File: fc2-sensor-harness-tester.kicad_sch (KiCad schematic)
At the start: 29 parts, among them J1 Conn_01x03_Pin, J105 CTRL INPUT (0-24VDC), J2 Conn_01x03_Pin, J201 0-10V DIM +, J203 V_IN (-) / 0-10V (-), Q203 BC858, Q205 DZT2222A

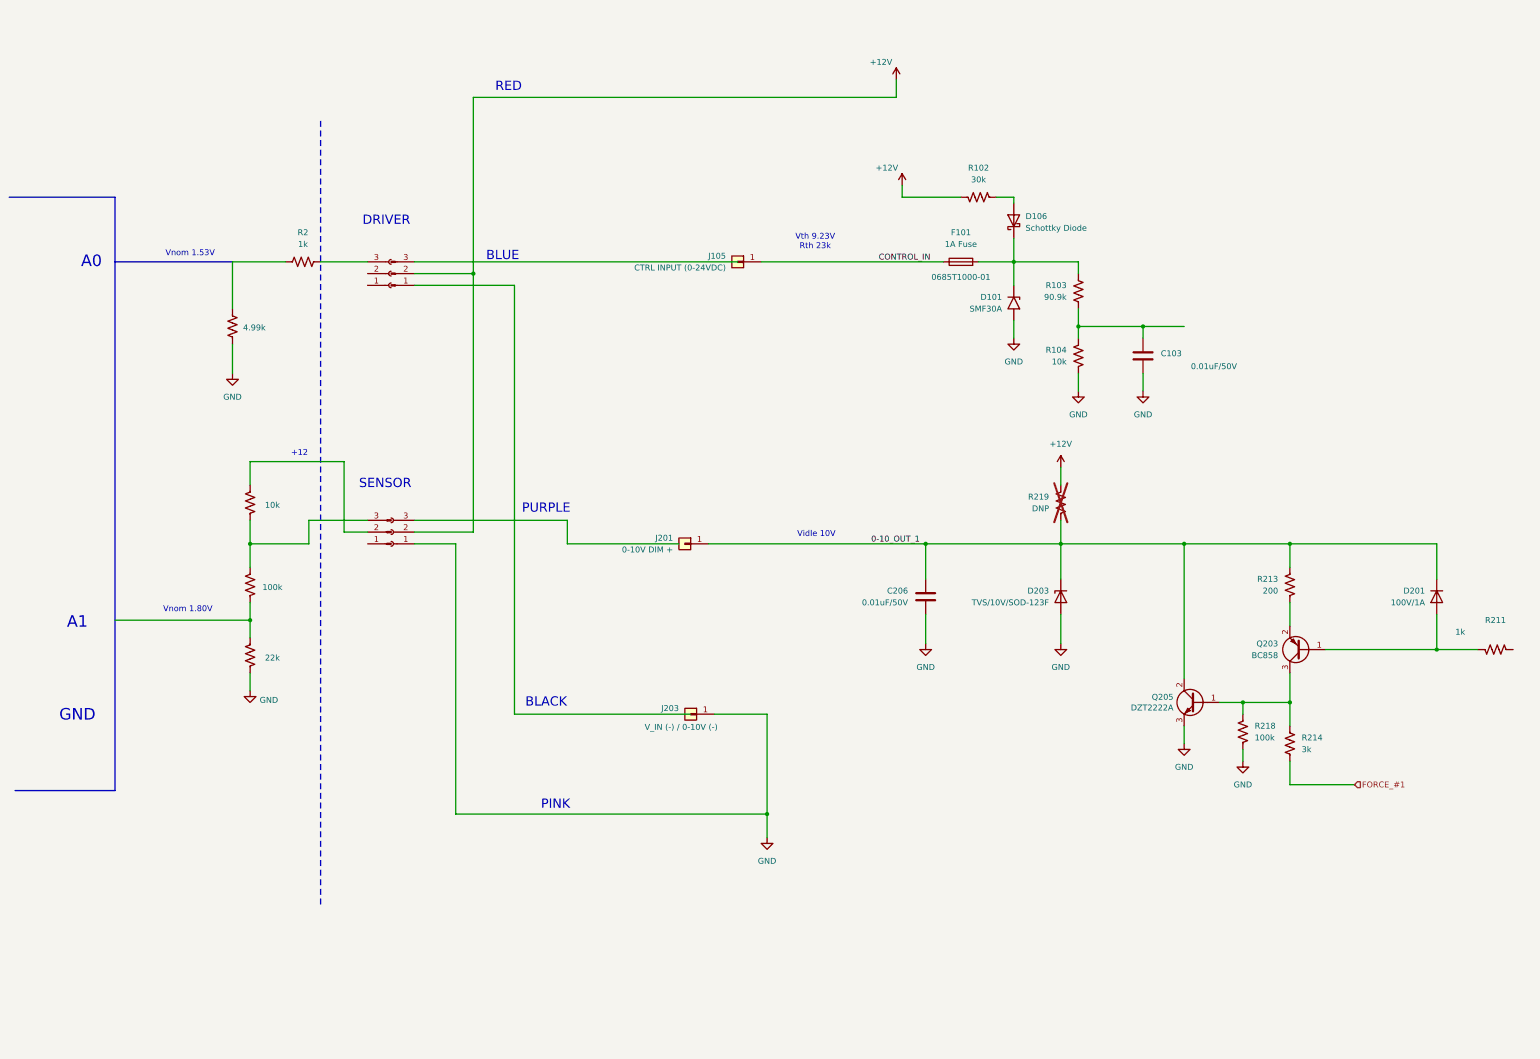
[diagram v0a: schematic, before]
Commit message: sense all pins, use int reference
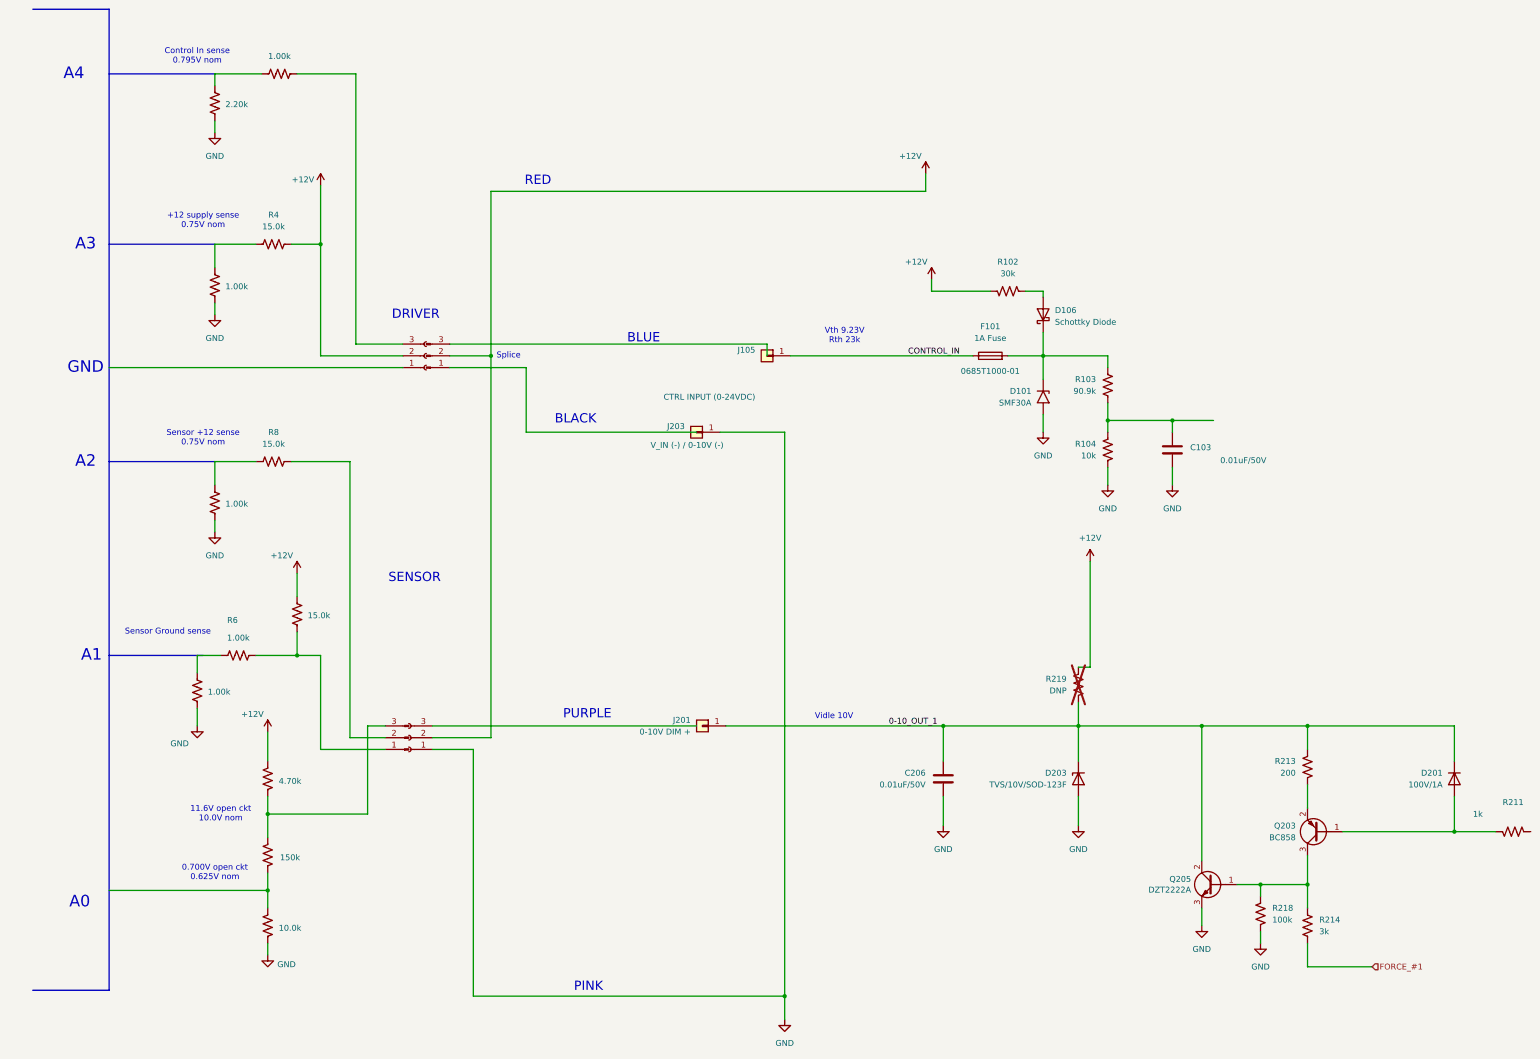
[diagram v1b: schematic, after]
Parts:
- added R10, R4, R8: 15.0k, symbol Device:R_US
- added R3, R5, R6, R7: 1.00k, symbol Device:R_US
- R1: value 4.99k -> 2.20k
- R105: value 10k -> 4.70k
- R106: value 100k -> 150k
- R107: value 22k -> 10.0k
- R2: value 1k -> 1.00k
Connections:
- net +12V: now also J3.2 (Pin_2), R105.1, R10.1, R4.2
- net GND: now also R3.2, R5.2, R7.2
- net at J2.2 (Pin_2): now also R8.2; no longer R105.1
- net at J2.1 (Pin_1): now also R10.2, R6.2
- new net: R5.1, R6.1
- new net: R7.1, R8.1
- new net: R3.1, R4.1
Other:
- note added: "+12 supply sense 0.75V nom"
- note added: "0.700V open ckt 0.625V nom"
- note added: "11.6V open ckt 10.0V nom"
- note added: "A2"
- note added: "A3"
- note added: "A4"
- note added: "Control In sense 0.795V nom"
- note added: "Sensor +12 sense 0.75V nom"
- note added: "Sensor Ground sense"
- note added: "Splice"
- note removed: "+12"
- note removed: "Vnom 1.53V"
- note removed: "Vnom 1.80V"
- moved on the sheet: C103, C206, D101, D106, D201, D203, F101, J105, J201, J203, Q203, Q205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

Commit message: more competent tester, update schematic
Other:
- note added: "A5"
- note added: "A6"
- note added: "A7"
- note removed: "A0"
- note removed: "A1"
- note removed: "A2"
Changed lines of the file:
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@@
 	(generator_version "10.0")
 	(paper "B")
-	(text "A2"
+	(text "A5"
 		(exclude_from_sim no)
 		(at 40.64 118.11 0)
@@
 		)
 	)
-	(text "A3"
+	(text "A6"
 		(exclude_from_sim no)
 		(at 40.64 71.12 0)
@@
 	(text "DRIVER"
 		(exclude_from_sim no)
-		(at 112.014 86.36 0)
+		(at 110.236 168.656 0)
 		(effects
 			(font
@@
 		)
 	)
-	(text "A1"
+	(text "A4"
 		(exclude_from_sim no)
 		(at 41.91 160.02 0)
@@
 		)
 	)
-	(text "A4"
+	(text "A7"
 		(exclude_from_sim no)
 		(at 38.1 34.29 0)
@@
 	(text "SENSOR"
 		(exclude_from_sim no)
-		(at 111.76 143.256 0)
+		(at 114.808 86.36 0)
 		(effects
 			(font
@@
 		)
 	)
-	(text "A0"
+	(text "A3"
 		(exclude_from_sim no)
 		(at 39.37 213.36 0)
